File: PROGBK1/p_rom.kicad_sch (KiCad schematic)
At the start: 43 parts, among them J10 J10, J11 J11, J12 J12, J13 J13, J3 J3, J4 J4, J5 J5, J6 J6, J7 J7, J8 J8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

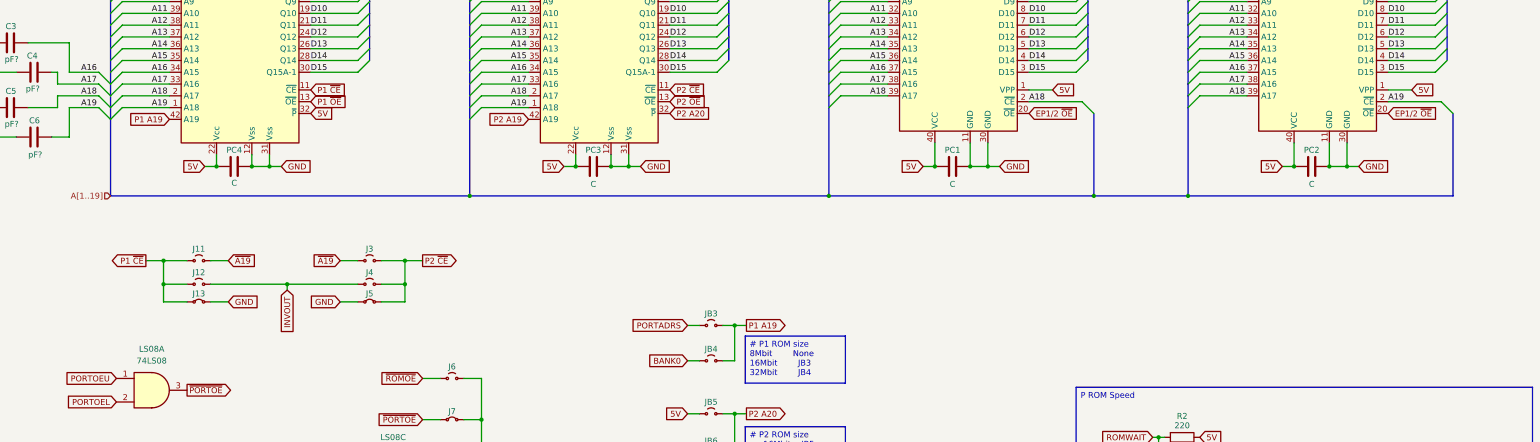
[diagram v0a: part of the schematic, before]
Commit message: Minor change to EP-rom pins
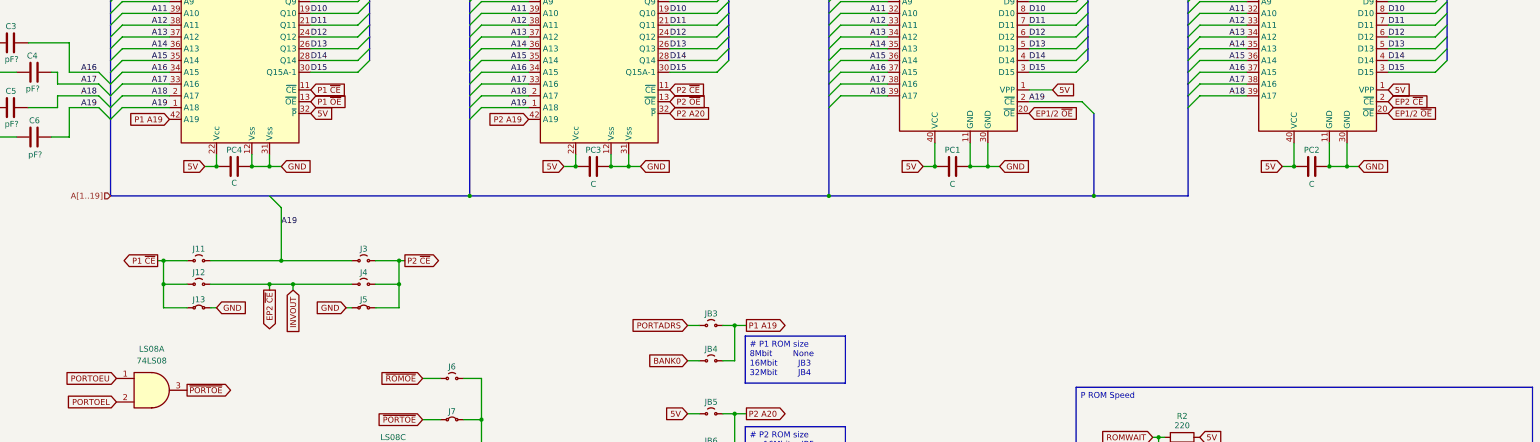
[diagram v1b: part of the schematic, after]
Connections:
- net ~{A19} is gone; now on net A19: J11.1 (A), J3.1 (A)
- net A18: no longer EP1.2 (~{CE})
- net A19: now also EP1.2 (~{CE}); no longer EP2.2 (~{CE})
- net INVOUT renamed EP2 ~{CE}
- net EP2 ~{CE}: now also EP2.2 (~{CE})
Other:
- moved on the sheet: J13, J3, J4, J5

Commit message: Updated schematics and PCB layout
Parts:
- C3, C4, C5, C6, PC1, PC2, PC3, PC4: footprint (none) -> Capacitor_SMD:C_0805_2012Metric_Pad1.18x1.45mm_HandSolder
- EP1, EP2: footprint (none) -> Package_DIP:DIP-40_W15.24mm_Socket_LongPads
- J1: renamed from JP36; footprint (none) -> Resistor_SMD:R_1206_3216Metric_Pad1.30x1.75mm_HandSolder
- J10, J11, J12, J13, J3, J4, J5, J6, J7, J8, J9, JB1, JB2, JB3, JB4, JB5, JB6, R2, R3, R4, R5, R6, R7: footprint (none) -> Resistor_SMD:R_1206_3216Metric_Pad1.30x1.75mm_HandSolder
- J2: renamed from JP37; footprint (none) -> Resistor_SMD:R_1206_3216Metric_Pad1.30x1.75mm_HandSolder
- LS08, LS74: footprint (none) -> Package_SO:SO-14_5.3x10.2mm_P1.27mm
- LS139: footprint (none) -> Package_SO:SO-16_5.3x10.2mm_P1.27mm
- P1, SP2: footprint (none) -> Package_DIP:DIP-42_W15.24mm_Socket_LongPads
- PC10: renamed from PC13; footprint (none) -> Capacitor_SMD:C_0805_2012Metric_Pad1.18x1.45mm_HandSolder
- PC11: renamed from PC14; footprint (none) -> Capacitor_SMD:C_0805_2012Metric_Pad1.18x1.45mm_HandSolder
- PC12: renamed from PC15; footprint (none) -> Capacitor_SMD:C_0805_2012Metric_Pad1.18x1.45mm_HandSolder
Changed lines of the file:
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@@
 			)
 		)
-		(property "Footprint" ""
+		(property "Footprint" "Capacitor_SMD:C_0805_2012Metric_Pad1.18x1.45mm_HandSolder"
 			(at 326.39 134.3152 0)
 			(effects
@@
 			)
 		)
-		(property "Footprint" ""
+		(property "Footprint" "Package_SO:SO-14_5.3x10.2mm_P1.27mm"
 			(at 132.08 200.66 0)
 			(effects
@@
 		(on_board yes)
 		(dnp no)
-		(property "Reference" "PC14"
+		(property "Reference" "PC11"
 			(at 80.01 247.904 90)
 			(effects
@@
 			)
 		)
-		(property "Footprint" ""
+		(property "Footprint" "Capacitor_SMD:C_0805_2012Metric_Pad1.18x1.45mm_HandSolder"
 			(at 76.2 254.9652 0)
 			(effects
@@
 			(project "progbk1"
 				(path "/24b638d1-48d9-4353-ba58-4296637a547f/b7816910-99e2-4b63-b883-5ac2266ea859"
-					(reference "PC14")
+					(reference "PC11")
 					(unit 1)
 				)
@@
 			)
 		)
-		(property "Footprint" ""
+		(property "Footprint" "Capacitor_SMD:C_0805_2012Metric_Pad1.18x1.45mm_HandSolder"
 			(at 248.92 134.3152 0)
 			(effects
@@
 			)
 		)
-		(property "Footprint" ""
+		(property "Footprint" "Resistor_SMD:R_1206_3216Metric_Pad1.30x1.75mm_HandSolder"
 			(at 302.26 199.39 0)
 			(effects
@@
 		(on_board yes)
 		(dnp no)
-		(property "Reference" "JP37"
-			(at 292.1 54.356 0)
+		(property "Reference" "J2"
+			(at 292.1 57.15 0)
 			(effects
 				(font
@@
 					(size 1.27 1.27)
 				)
+				(hide yes)
 			)
 		)
-		(property "Footprint" ""
+		(property "Footprint" "Resistor_SMD:R_1206_3216Metric_Pad1.30x1.75mm_HandSolder"
 			(at 292.1 59.69 0)
 			(effects
@@
 			(project "progbk1"
 				(path "/24b638d1-48d9-4353-ba58-4296637a547f/b7816910-99e2-4b63-b883-5ac2266ea859"
-					(reference "JP37")
+					(reference "J2")
 					(unit 1)
 				)
@@
 			)
 		)
-		(property "Footprint" ""
+		(property "Footprint" "Resistor_SMD:R_1206_3216Metric_Pad1.30x1.75mm_HandSolder"
 			(at 144.78 236.22 0)
 			(effects
@@
 			)
 		)
-		(property "Footprint" ""
+		(property "Footprint" "Capacitor_SMD:C_0805_2012Metric_Pad1.18x1.45mm_HandSolder"
 			(at 45.72 107.6452 0)
 			(effects
@@
 			)
 		)
-		(property "Footprint" ""
+		(property "Footprint" "Capacitor_SMD:C_0805_2012Metric_Pad1.18x1.45mm_HandSolder"
 			(at 171.45 134.3152 0)
 			(effects
@@
 			)
 		)
-		(property "Footprint" ""
+		(property "Footprint" "Resistor_SMD:R_1206_3216Metric_Pad1.30x1.75mm_HandSolder"
 			(at 90.17 158.75 0)
 			(effects
@@
 			)
 		)
-		(property "Footprint" ""
+		(property "Footprint" "Resistor_SMD:R_1206_3216Metric_Pad1.30x1.75mm_HandSolder"
 			(at 144.78 245.11 0)
 			(effects
@@
 			)
 		)
-		(property "Footprint" ""
+		(property "Footprint" "Package_SO:SO-14_5.3x10.2mm_P1.27mm"
 			(at 204.47 242.57 0)
 			(effects
@@
 			)
 		)
-		(property "Footprint" ""
+		(property "Footprint" "Resistor_SMD:R_1206_3216Metric_Pad1.30x1.75mm_HandSolder"
 			(at 200.66 194.31 0)
 			(effects
@@
 			)
 		)
-		(property "Footprint" ""
+		(property "Footprint" "Resistor_SMD:R_1206_3216Metric_Pad1.30x1.75mm_HandSolder"
 			(at 200.66 167.64 0)
 			(effects
@@
 			)
 		)
-		(property "Footprint" ""
+		(property "Footprint" "Resistor_SMD:R_1206_3216Metric_Pad1.30x1.75mm_HandSolder"
 			(at 302.26 212.852 90)
 			(effects
@@
 			)
 		)
-		(property "Footprint" ""
+		(property "Footprint" "Package_SO:SO-14_5.3x10.2mm_P1.27mm"
 			(at 80.01 181.61 0)
 			(effects
@@
 			)
 		)
-		(property "Footprint" ""
+		(property "Footprint" "Package_SO:SO-14_5.3x10.2mm_P1.27mm"
 			(at 45.72 274.32 0)
 			(effects
@@
 		(on_board yes)
 		(dnp no)
-		(property "Reference" "PC15"
+		(property "Reference" "PC12"
 			(at 80.01 258.064 90)
 			(effects
@@
 			)
 		)
-		(property "Footprint" ""
+		(property "Footprint" "Capacitor_SMD:C_0805_2012Metric_Pad1.18x1.45mm_HandSolder"
 			(at 76.2 265.1252 0)
 			(effects
@@
 			(project "progbk1"
 				(path "/24b638d1-48d9-4353-ba58-4296637a547f/b7816910-99e2-4b63-b883-5ac2266ea859"
-					(reference "PC15")
+					(reference "PC12")
 					(unit 1)
 				)
@@
 			)
 		)
-		(property "Footprint" ""
+		(property "Footprint" "Resistor_SMD:R_1206_3216Metric_Pad1.30x1.75mm_HandSolder"
 			(at 302.26 220.472 90)
 			(effects
@@
 			)
 		)
-		(property "Footprint" ""
+		(property "Footprint" "Package_SO:SO-16_5.3x10.2mm_P1.27mm"
 			(at 45.72 234.95 0)
 			(effects
@@
 			)
 		)
-		(property "Footprint" ""
+		(property "Footprint" "Capacitor_SMD:C_0805_2012Metric_Pad1.18x1.45mm_HandSolder"
 			(at 45.72 121.6152 0)
 			(effects
@@
 			)
 		)
-		(property "Footprint" ""
+		(property "Footprint" "Package_DIP:DIP-40_W15.24mm_Socket_LongPads"
 			(at 246.38 81.28 0)
 			(effects
@@
 			)
 		)
-		(property "Footprint" ""
+		(property "Footprint" "Capacitor_SMD:C_0805_2012Metric_Pad1.18x1.45mm_HandSolder"
 			(at 50.8 127.9652 0)
 			(effects
@@
 			)
 		)
-		(property "Footprint" ""
+		(property "Footprint" "Package_DIP:DIP-42_W15.24mm_Socket_LongPads"
 			(at 91.44 81.28 0)
 			(effects
@@
 			)
 		)
-		(property "Footprint" ""
+		(property "Footprint" "Resistor_SMD:R_1206_3216Metric_Pad1.30x1.75mm_HandSolder"
 			(at 90.17 153.67 0)
 			(effects
@@
 			)
 		)
-		(property "Footprint" ""
+		(property "Footprint" "Package_SO:SO-14_5.3x10.2mm_P1.27mm"
 			(at 204.47 217.17 0)
 			(effects
@@
 			)
 		)
-		(property "Footprint" ""
+		(property "Footprint" "Package_SO:SO-14_5.3x10.2mm_P1.27mm"
 			(at 132.08 236.22 0)
 			(effects
@@
 		(on_board yes)
 		(dnp no)
-		(property "Reference" "JP36"
-			(at 292.1 47.498 0)
+		(property "Reference" "J1"
+			(at 292.1 50.292 0)
 			(effects
 				(font
@@
 					(size 1.27 1.27)
 				)
+				(hide yes)
 			)
 		)
-		(property "Footprint" ""
+		(property "Footprint" "Resistor_SMD:R_1206_3216Metric_Pad1.30x1.75mm_HandSolder"
 			(at 292.1 52.07 0)
 			(effects
@@
 			(project "progbk1"
 				(path "/24b638d1-48d9-4353-ba58-4296637a547f/b7816910-99e2-4b63-b883-5ac2266ea859"
-					(reference "JP36")
+					(reference "J1")
 					(unit 1)
 				)
@@
 			)
 		)
-		(property "Footprint" ""
+		(property "Footprint" "Resistor_SMD:R_1206_3216Metric_Pad1.30x1.75mm_HandSolder"
 			(at 125.73 163.83 0)
 			(effects
@@
 		(on_board yes)
 		(dnp no)
-		(property "Reference" "PC13"
+		(property "Reference" "PC10"
 			(at 80.01 237.744 90)
 			(effects
@@
 			)
 		)
-		(property "Footprint" ""
+		(property "Footprint" "Capacitor_SMD:C_0805_2012Metric_Pad1.18x1.45mm_HandSolder"
 			(at 76.2 244.8052 0)
 			(effects
@@
 			(project "progbk1"
 				(path "/24b638d1-48d9-4353-ba58-4296637a547f/b7816910-99e2-4b63-b883-5ac2266ea859"
-					(reference "PC13")
+					(reference "PC10")
 					(unit 1)
 				)
@@
 			)
 		)
-		(property "Footprint" ""
+		(property "Footprint" "Resistor_SMD:R_1206_3216Metric_Pad1.30x1.75mm_HandSolder"
 			(at 90.17 163.83 0)
 			(effects
@@
 			)
 		)
-		(property "Footprint" ""
+		(property "Footprint" "Resistor_SMD:R_1206_3216Metric_Pad1.30x1.75mm_HandSolder"
 			(at 125.73 158.75 0)
 			(effects
@@
 			)
 		)
-		(property "Footprint" ""
+		(property "Footprint" "Resistor_SMD:R_1206_3216Metric_Pad1.30x1.75mm_HandSolder"
 			(at 144.78 215.9 0)
 			(effects
@@
 			)
 		)
-		(property "Footprint" ""
+		(property "Footprint" "Resistor_SMD:R_1206_3216Metric_Pad1.30x1.75mm_HandSolder"
 			(at 144.78 224.79 0)
 			(effects
@@
 			)
 		)
-		(property "Footprint" ""
+		(property "Footprint" "Package_DIP:DIP-40_W15.24mm_Socket_LongPads"
 			(at 323.85 81.28 0)
 			(effects
@@
 			)
 		)
-		(property "Footprint" ""
+		(property "Footprint" "Package_SO:SO-14_5.3x10.2mm_P1.27mm"
 			(at 45.72 254 0)
 			(effects
@@
 			)
 		)
-		(property "Footprint" ""
+		(property "Footprint" "Resistor_SMD:R_1206_3216Metric_Pad1.30x1.75mm_HandSolder"
 			(at 200.66 175.26 0)
 			(effects
@@
 			)
 		)
-		(property "Footprint" ""
+		(property "Footprint" "Resistor_SMD:R_1206_3216Metric_Pad1.30x1.75mm_HandSolder"
 			(at 302.26 207.01 0)
 			(effects
@@
 			)
 		)
-		(property "Footprint" ""
+		(property "Footprint" "Package_SO:SO-16_5.3x10.2mm_P1.27mm"
 			(at 83.82 207.01 0)
 			(effects
@@
 			)
 		)
-		(property "Footprint" ""
+		(property "Footprint" "Resistor_SMD:R_1206_3216Metric_Pad1.30x1.75mm_HandSolder"
 			(at 200.66 186.69 0)
 			(effects
@@
 			)
 		)
-		(property "Footprint" ""
+		(property "Footprint" "Resistor_SMD:R_1206_3216Metric_Pad1.30x1.75mm_HandSolder"
 			(at 144.78 179.07 0)
 			(effects
@@
 			)
 		)
-		(property "Footprint" ""
+		(property "Footprint" "Resistor_SMD:R_1206_3216Metric_Pad1.30x1.75mm_HandSolder"
 			(at 125.73 153.67 0)
 			(effects
@@
 			)
 		)
-		(property "Footprint" ""
+		(property "Footprint" "Capacitor_SMD:C_0805_2012Metric_Pad1.18x1.45mm_HandSolder"
 			(at 58.42 112.0648 0)
 			(effects
@@
 			)
 		)
-		(property "Footprint" ""
+		(property "Footprint" "Resistor_SMD:R_1206_3216Metric_Pad1.30x1.75mm_HandSolder"
 			(at 144.78 200.66 0)
 			(effects
@@
 			)
 		)
-		(property "Footprint" ""
+		(property "Footprint" "Resistor_SMD:R_1206_3216Metric_Pad1.30x1.75mm_HandSolder"
 			(at 222.25 230.378 90)
 			(effects
@@
 			)
 		)
-		(property "Footprint" ""
+		(property "Footprint" "Resistor_SMD:R_1206_3216Metric_Pad1.30x1.75mm_HandSolder"
 			(at 144.78 187.96 0)
 			(effects
@@
 			)
 		)
-		(property "Footprint" ""
+		(property "Footprint" "Package_DIP:DIP-42_W15.24mm_Socket_LongPads"
 			(at 168.91 81.28 0)
 			(effects
@@
 			)
 		)
-		(property "Footprint" ""
+		(property "Footprint" "Package_SO:SO-14_5.3x10.2mm_P1.27mm"
 			(at 132.08 215.9 0)
 			(effects
@@
 			)
 		)
-		(property "Footprint" ""
+		(property "Footprint" "Capacitor_SMD:C_0805_2012Metric_Pad1.18x1.45mm_HandSolder"
 			(at 93.98 134.3152 0)
 			(effects
@@
 			)
 		)
-		(property "Footprint" ""
+		(property "Footprint" "Resistor_SMD:R_1206_3216Metric_Pad1.30x1.75mm_HandSolder"
 			(at 302.26 189.992 90)
 			(effects
